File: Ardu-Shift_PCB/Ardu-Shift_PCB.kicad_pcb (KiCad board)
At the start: 2 copper layers, 101.6 x 66 mm, 18 parts, among them U1 OLED(SPI), U2 Arduino_Pro_Micro, U3 SPDT_Slide

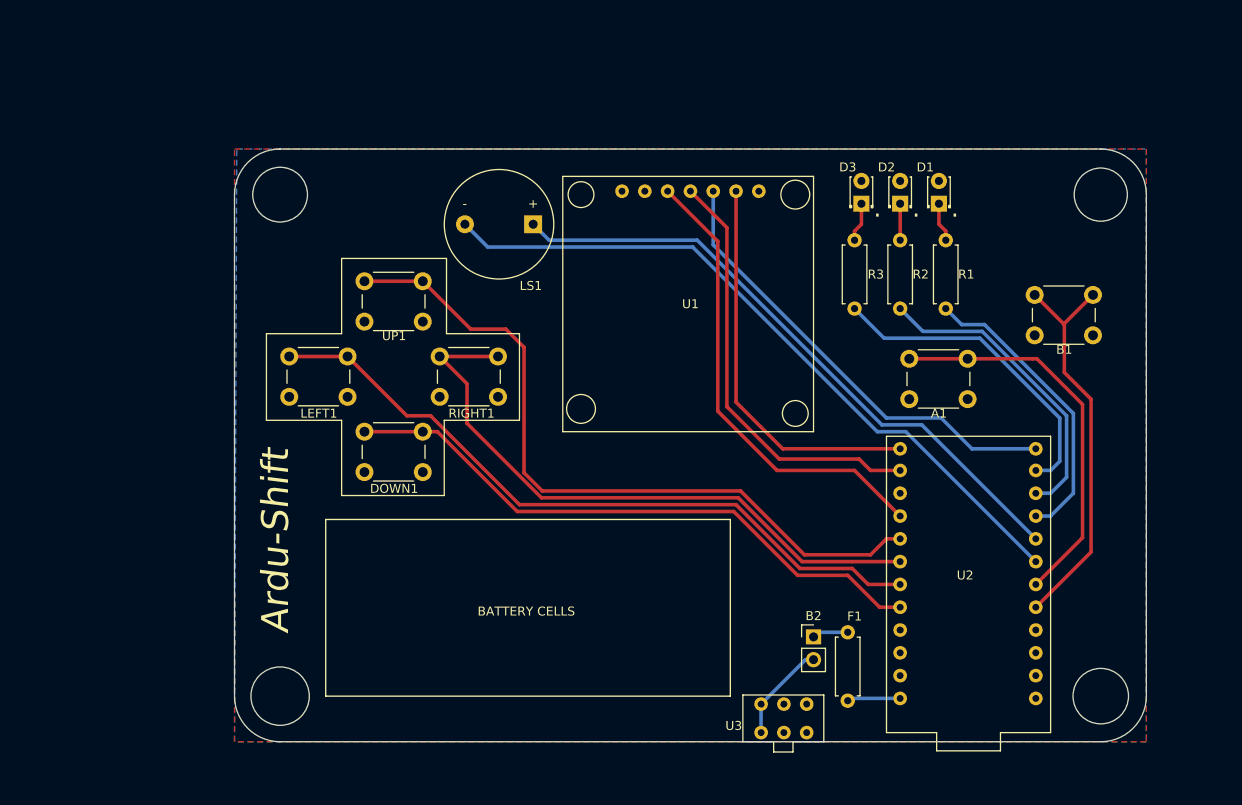
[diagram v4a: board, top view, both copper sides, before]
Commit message: swapped pins on schematic/PCB to work with arduboy library
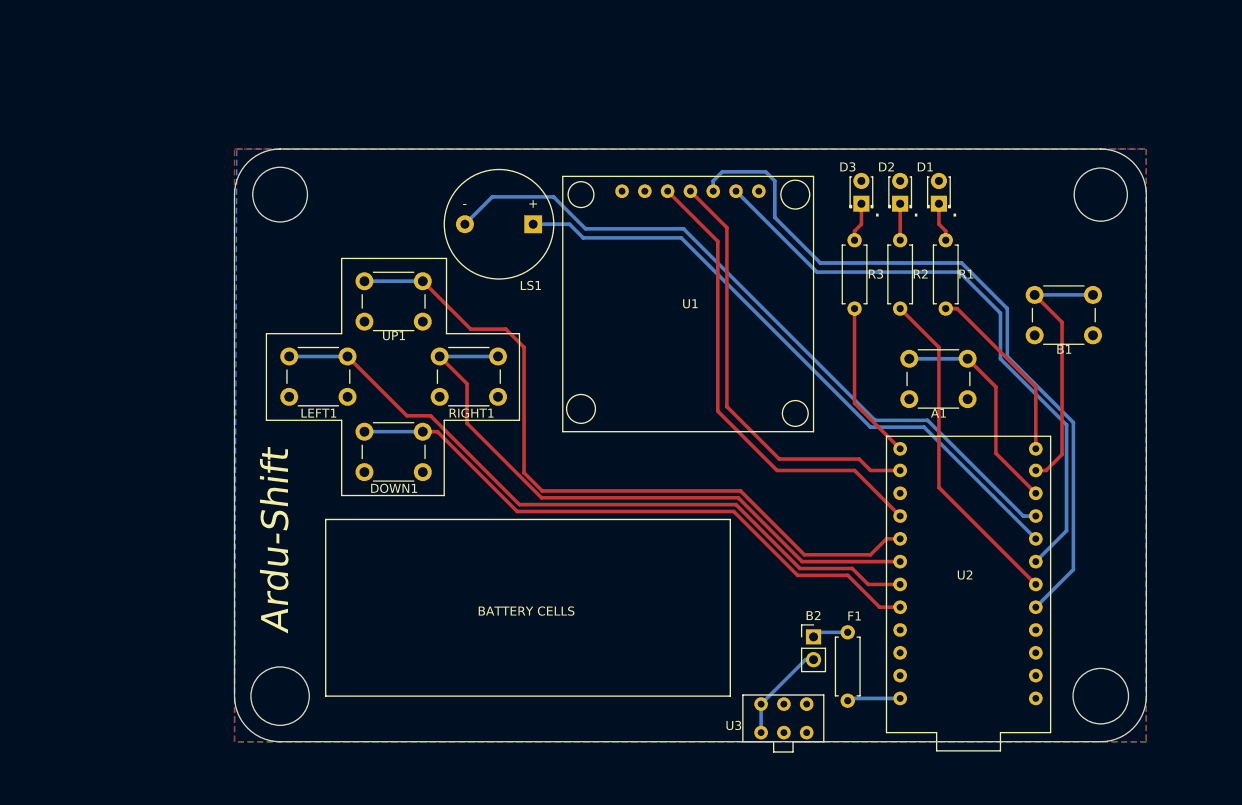
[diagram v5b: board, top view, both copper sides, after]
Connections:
- LEFT1 pad 1: Net-(LEFT1-Pad1) -> LEFT
- LEFT1 pad 2: Net-(LEFT1-Pad2) -> GND
- RIGHT1 pad 1: Net-(RIGHT1-Pad1) -> RIGHT
- RIGHT1 pad 2: Net-(RIGHT1-Pad2) -> GND
- U2 pad 10: CE -> R_LED
- U2 pad 2: B_Button -> RES
- U2 pad 3: A_Button -> G_LED
- U2 pad 4: Speaker- -> CE
- U2 pad 6: B_LED -> Speaker-
- U2 pad 7: G_LED -> A_Button
- U2 pad 8: R_LED -> B_Button
- U2 pad 9: RES -> B_LED
- UP1 pad 2: Net-(UP1-Pad2) -> GND
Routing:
- net RES: track 51.3 -> 81.1 mm
- net CE: track 43.9 -> 67.3 mm
- net A_Button: track 43.6 -> 24.6 mm
- net R_LED: track 35.8 -> 17.7 mm
- net B_Button: track 44.6 -> 29.2 mm
- net B_LED: track 33.2 -> 20.5 mm
- net G_LED: track 34.5 -> 37.0 mm

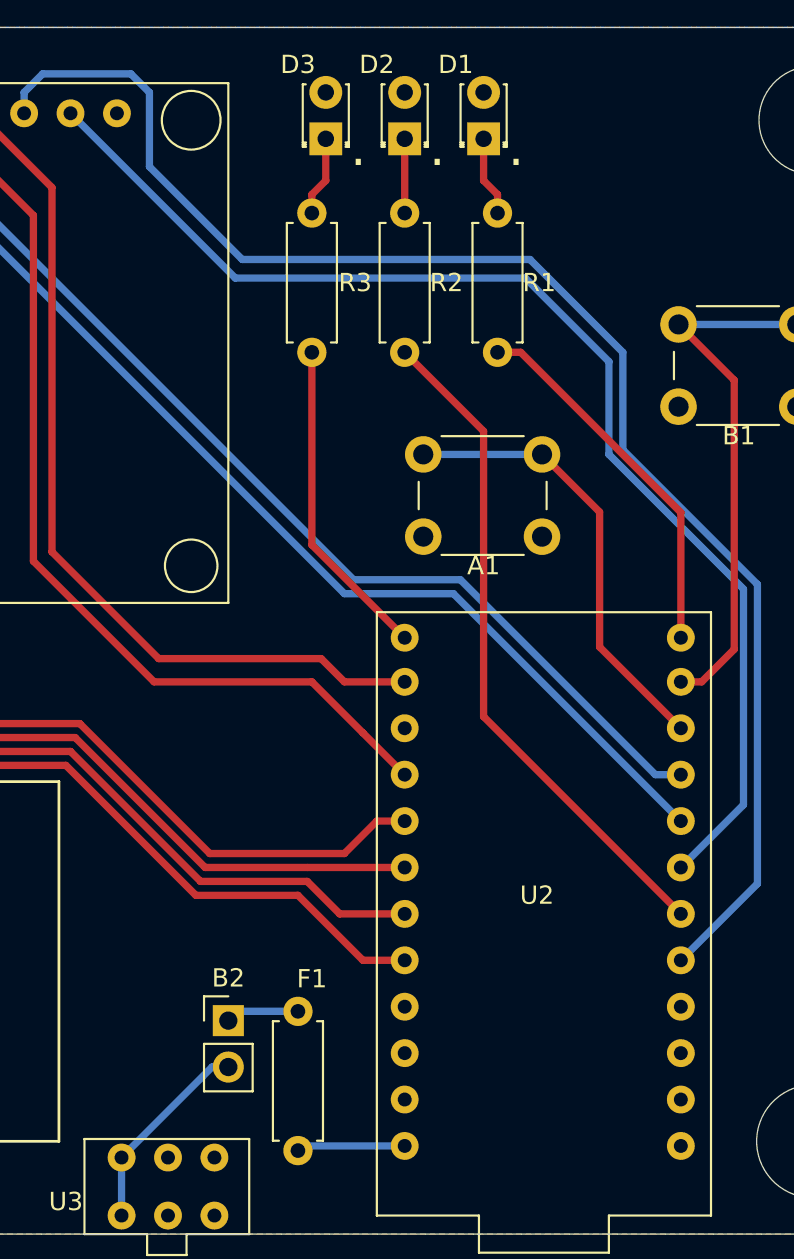
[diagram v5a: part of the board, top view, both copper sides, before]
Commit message: Updated PCB wiring, swapped some pins required for the 7-pin OLED to work with arduboy library
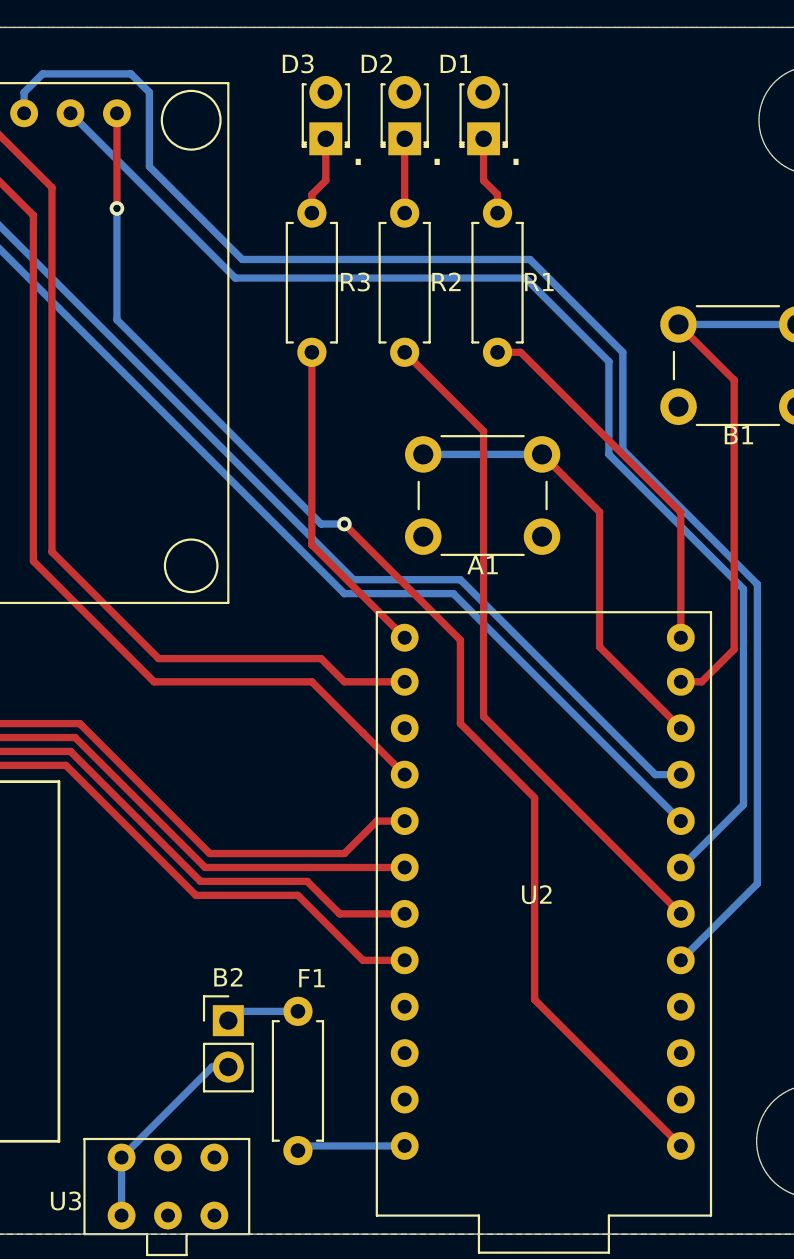
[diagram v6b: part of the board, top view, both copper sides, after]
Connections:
- net +5V renamed VCC
- net CE renamed DC
- U1 pad CS: GND -> CS
- U2 pad 1: Net-(U2-Pad1) -> CS
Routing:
- net CS: track 0.00 -> 70.0 mm, vias 0 -> 2

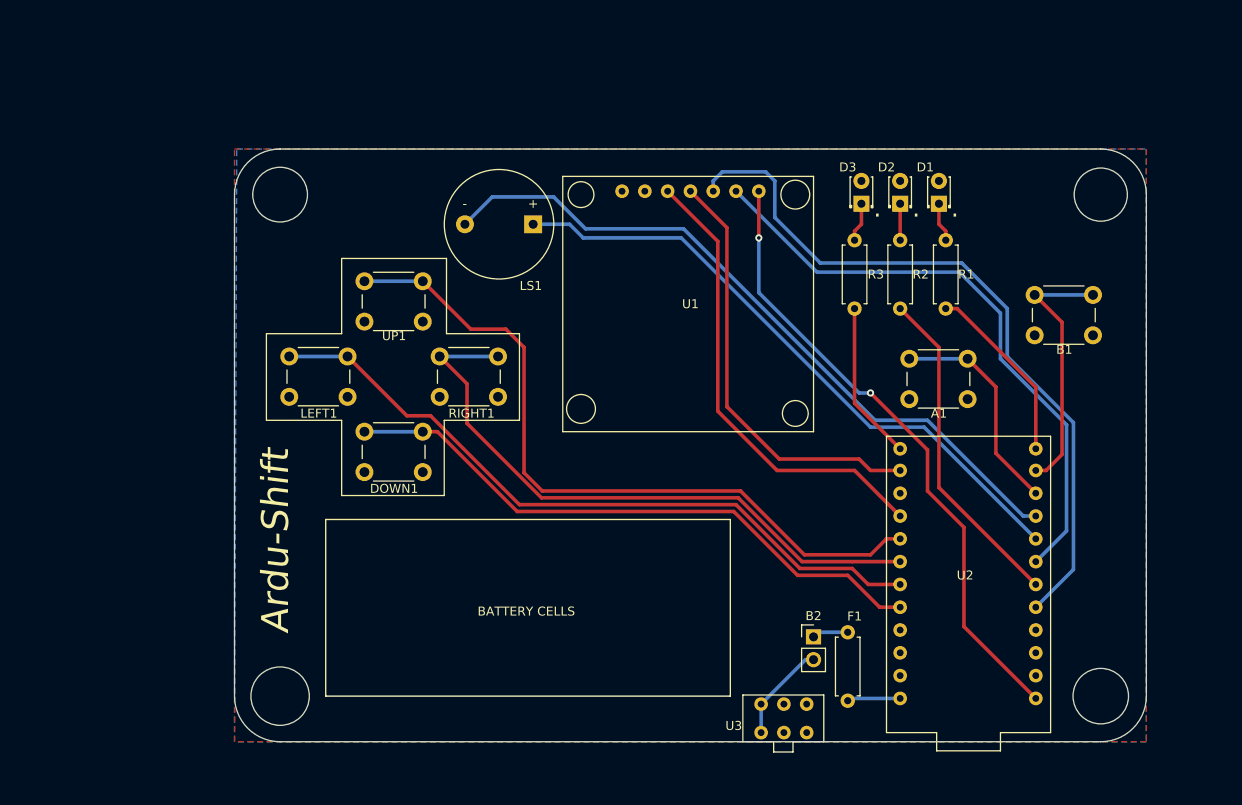
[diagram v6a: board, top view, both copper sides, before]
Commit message: finalized PCB design - ready for final review by team members. Gerber files generated for manufacturing
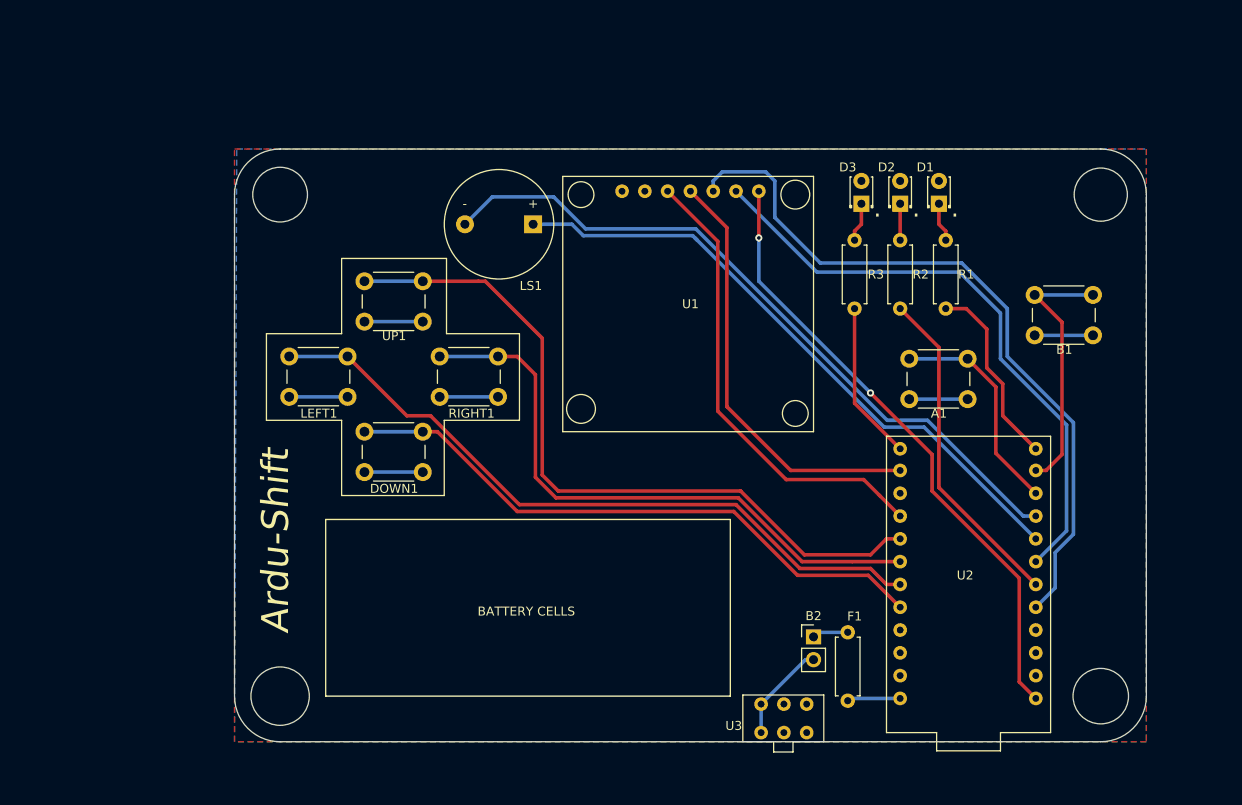
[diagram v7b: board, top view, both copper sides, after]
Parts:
- R1, R2: value R -> 470R
- R3: value R -> 220R
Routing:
- net GND: track 0.00 -> 39.0 mm
- net RIGHT: track 69.9 -> 67.5 mm
- net UP: track 81.2 -> 82.0 mm
- net CS: track 70.0 -> 69.3 mm
- net B_LED: track 20.5 -> 21.1 mm
